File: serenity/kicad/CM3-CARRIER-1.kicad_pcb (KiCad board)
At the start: 4 copper layers, 68 x 30 mm, 22 parts, among them J1 SODIMM-200-CM3+, U1 MCP2518FD, U1B ATA6561, U2 MAX3485E, U3 HI-6130, U4 W5500, U5 CH340C, U6 AP2112K-3.3, U7 CAT24C32

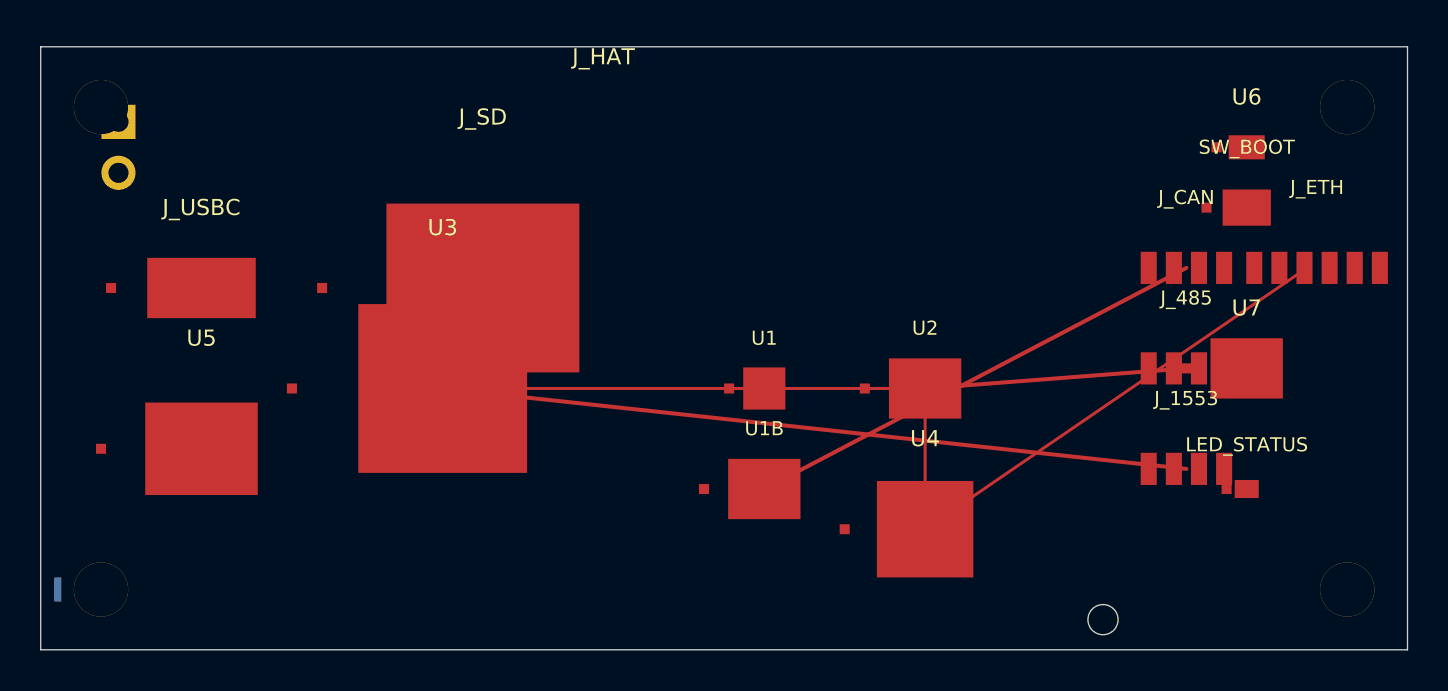
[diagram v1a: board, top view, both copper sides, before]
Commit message: Replace generic PCB silk labels with short descriptive names
Update all F.SilkS/B.SilkS fp_text reference labels across 7 KiCad PCB
files, replacing J/U/T numeric designators with function-based names so
each component is identifiable on the board without a BOM lookup.

CAPE-A-1 / CAPE-A-1-no-comment:
  J1→PB2-P1, J2→PB2-P2, U1→IMU, U2→BARO, U3→GPS,
  U4/U5→CAN-TR/RS485, U6→1553-DRV, U7→1553-RCV, T1→1553-XFM,
  U8/U9→ETH1-PHY/ETH2-PHY, U10→TPM,
  J3→CAN-FD, J4→RS-485, J5→MIL-1553, J6→ETH1, J7→ETH2,
  J8→ESC-TLM, J9→SERVO, J10→PWR-IN

CAPE-B-1 (adds RF + payload peripherals):
  U1→LORA, U2→WIFI-BT, U10→SD-WB, U11→NOR-FLASH,
  U12→WINCH-DRV, U13→LOAD-ADC, U14→PWM-I2C,
  J8→SIK-TLM, J9→RC-RCVR, J11→WINCH, J12→LOAD-CELL, J13→NAV-LIGHT

COMMS-HAT-1 (connectors + crystal only; ICs already descriptive):
  J1→SIK-UART, J2→ETH, J3→GPIO-EXT, J4→CAN-FD,
  JP4→PWR-IN, Y1→ETH-CLK

COMMS-HAT-SWITCH:
  Y1→SW-CLK

TRIHAT-1 (superseded; ICs + inferred connector mapping):
  U1→IMU, U2→BARO, U3→GPS, U4→CAN-CTRL, U5→CAN-TR,
  U6→ETH-CTRL, U7→ETH-MAG, U8→TPM, U9→LDO, Y1→ETH-CLK,
  J-connectors mapped from net list (GPS/CAN-FD/ETH/ESC-OUT/SERVO-OUT/etc.)

CM3-CARRIER-1:
  J1→CM3-SDIMM, U1→CAN-CTRL, U1B→CAN-TR, U2→RS485,
  U3→MIL-1553, U4→ETH-CTRL, U5→USB-UART, U6→LDO, U7→HAT-EEPROM

Boards already fully descriptive (SENSORHAT-1, CM4-CARRIER-1,
CM4-CARRIER-2) are unchanged.

https://claude.ai/code/session_01GniMw4QukTVM7JMzyVjH6p
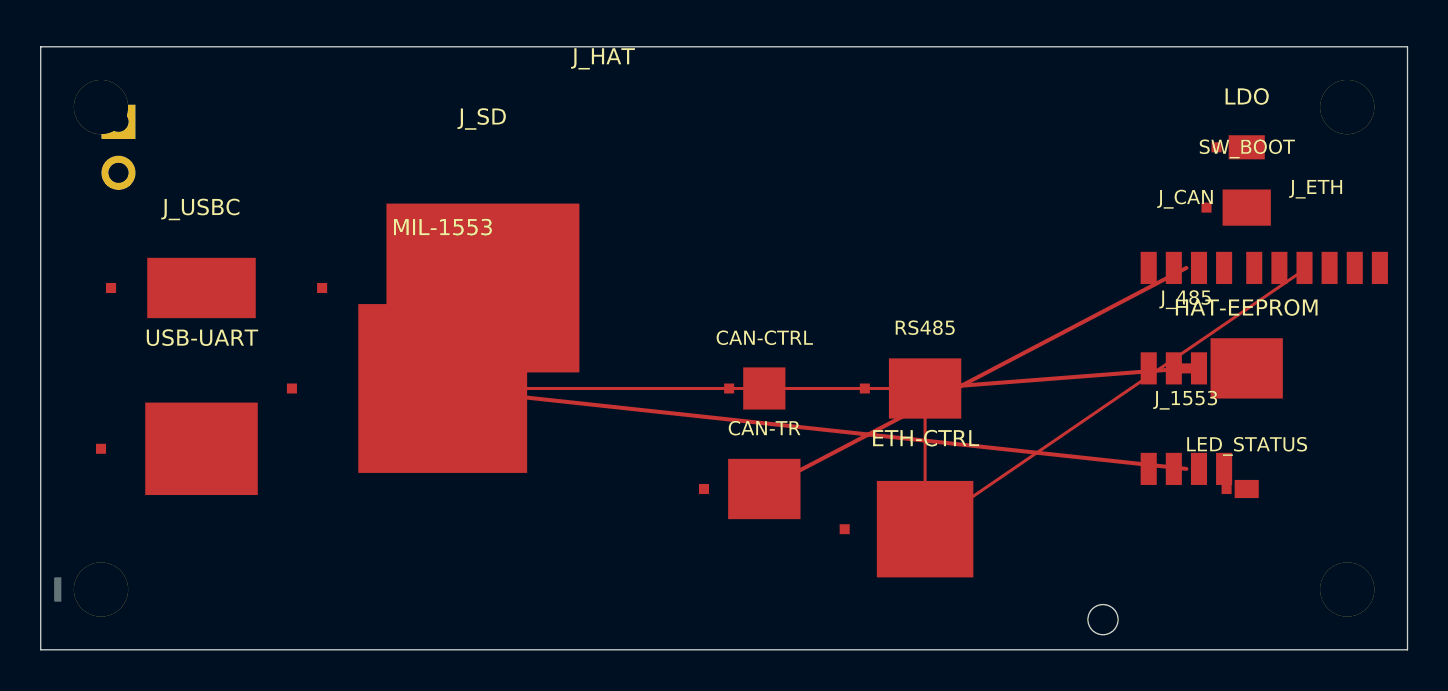
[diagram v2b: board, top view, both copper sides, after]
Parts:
- removed J1: SODIMM-200-CM3+, SODIMM_200pin_0.6mm
- removed U1: MCP2518FD, Package
- removed U1B: ATA6561, Package
- removed U2: MAX3485E, Package
- removed U3: HI-6130, Package
- removed U4: W5500, Package
- removed U5: CH340C, Package
- removed U6: AP2112K-3.3, Package
- removed U7: CAT24C32, Package
- added CAN-CTRL: MCP2518FD, Package, F.Cu at (36.0, 17.0)
- added CAN-TR: ATA6561, Package, F.Cu at (36.0, 22.0)
- added CM3-SDIMM: SODIMM-200-CM3+, SODIMM_200pin_0.6mm, B.Cu at (34.0, 28.5)
- added ETH-CTRL: W5500, Package, F.Cu at (44.0, 24.0)
- added HAT-EEPROM: CAT24C32, Package, F.Cu at (60.0, 16.0)
- added LDO: AP2112K-3.3, Package, F.Cu at (60.0, 5.00)
- added MIL-1553: HI-6130, Package, F.Cu at (20.0, 17.0)
- added RS485: MAX3485E, Package, F.Cu at (44.0, 17.0)
- added USB-UART: CH340C, Package, F.Cu at (8.00, 20.0)
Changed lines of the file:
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@@
   (footprint "SODIMM_200pin_0.6mm" (layer "B.Cu") (at 34 28.5)
     (property "Description" "RPi CM3/CM3+ 200-pin SODIMM edge connector (TE 1473005-4 or equiv)")
-    (fp_text reference "J1" (at 0 -4) (layer "B.SilkS")
+    (fp_text reference "CM3-SDIMM" (at 0 -4) (layer "B.SilkS")
       (effects (font (size 0.8 0.8) (thickness 0.12))))
     (fp_text value "SODIMM-200-CM3+" (at 0 4) (layer "B.Fab")
@@
   (footprint "Package" (layer "F.Cu") (at 36 17)
     (property "Description" "MCP2518FD CAN FD controller QFN-20 — SPI0 CS0 — ISO 11898-1:2015 1Mbit/s")
-    (fp_text reference "U1" (at 0 -2.5) (layer "F.SilkS")
+    (fp_text reference "CAN-CTRL" (at 0 -2.5) (layer "F.SilkS")
       (effects (font (size 0.7 0.7) (thickness 0.12))))
     (fp_text value "MCP2518FD" (at 0 2.5) (layer "F.Fab")
@@
   (footprint "Package" (layer "F.Cu") (at 36 22)
     (property "Description" "ATA6561 CAN FD transceiver SO-8 — 5Mbit/s — galv. capable")
-    (fp_text reference "U1B" (at 0 -3.0) (layer "F.SilkS")
+    (fp_text reference "CAN-TR" (at 0 -3.0) (layer "F.SilkS")
       (effects (font (size 0.7 0.7) (thickness 0.12))))
     (fp_text value "ATA6561" (at 0 3.0) (layer "F.Fab")
@@
   (footprint "Package" (layer "F.Cu") (at 44 17)
     (property "Description" "MAX3485E RS-485 transceiver SO-8 — 3.3V — half-duplex — 3Mbit/s")
-    (fp_text reference "U2" (at 0 -3.0) (layer "F.SilkS")
+    (fp_text reference "RS485" (at 0 -3.0) (layer "F.SilkS")
       (effects (font (size 0.7 0.7) (thickness 0.12))))
     (fp_text value "MAX3485E" (at 0 3.0) (layer "F.Fab")
@@
   (footprint "Package" (layer "F.Cu") (at 20 17)
     (property "Description" "HI-6130 MIL-STD-1553B RT controller LQFP-80 — SPI1 — 78ohm stub — galv. isolated")
-    (fp_text reference "U3" (at 0 -8.0) (layer "F.SilkS")
+    (fp_text reference "MIL-1553" (at 0 -8.0) (layer "F.SilkS")
       (effects (font (size 0.8 0.8) (thickness 0.15))))
     (fp_text value "HI-6130" (at 0 8.0) (layer "F.Fab")
@@
   (footprint "Package" (layer "F.Cu") (at 44 24)
     (property "Description" "W5500 Ethernet controller LQFP-48 — SPI0 CS1 — 100BASE-T — hardware TCP/IP stack")
-    (fp_text reference "U4" (at 0 -4.5) (layer "F.SilkS")
+    (fp_text reference "ETH-CTRL" (at 0 -4.5) (layer "F.SilkS")
       (effects (font (size 0.8 0.8) (thickness 0.15))))
     (fp_text value "W5500" (at 0 4.5) (layer "F.Fab")
@@
   (footprint "Package" (layer "F.Cu") (at 8 20)
     (property "Description" "CH340C USB-UART bridge SOP-16 — CM3+ UART0 programming/console — no crystal")
-    (fp_text reference "U5" (at 0 -5.5) (layer "F.SilkS")
+    (fp_text reference "USB-UART" (at 0 -5.5) (layer "F.SilkS")
       (effects (font (size 0.8 0.8) (thickness 0.15))))
     (fp_text value "CH340C" (at 0 5.5) (layer "F.Fab")
@@
   (footprint "Package" (layer "F.Cu") (at 60 5)
     (property "Description" "AP2112K-3.3 LDO 600mA SOT-25 — 5V to 3.3V — CM3+ IO + bus transceivers + HAT")
-    (fp_text reference "U6" (at 0 -2.5) (layer "F.SilkS")
+    (fp_text reference "LDO" (at 0 -2.5) (layer "F.SilkS")
       (effects (font (size 0.8 0.8) (thickness 0.15))))
     (fp_text value "AP2112K-3.3" (at 0 2.5) (layer "F.Fab")
@@
   (footprint "Package" (layer "F.Cu") (at 60 16)
     (property "Description" "CAT24C32WI 4Kbit I2C EEPROM SO-8 — RPi HAT ID at 0x50 on ID_SD/ID_SC")
-    (fp_text reference "U7" (at 0 -3.0) (layer "F.SilkS")
+    (fp_text reference "HAT-EEPROM" (at 0 -3.0) (layer "F.SilkS")
       (effects (font (size 0.8 0.8) (thickness 0.15))))
     (fp_text value "CAT24C32" (at 0 3.0) (layer "F.Fab")
